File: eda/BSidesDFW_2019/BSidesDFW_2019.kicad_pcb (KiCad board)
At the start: 2 copper layers, 33 x 43.5 mm, 28 parts, among them IC1 CH552G, J1 USB_B_Micro, J2 Test 1-8, J3 Test 9-16, J4 Battery, SW1 TS2306A, SW11 TS2306A, SW34 TS2306A

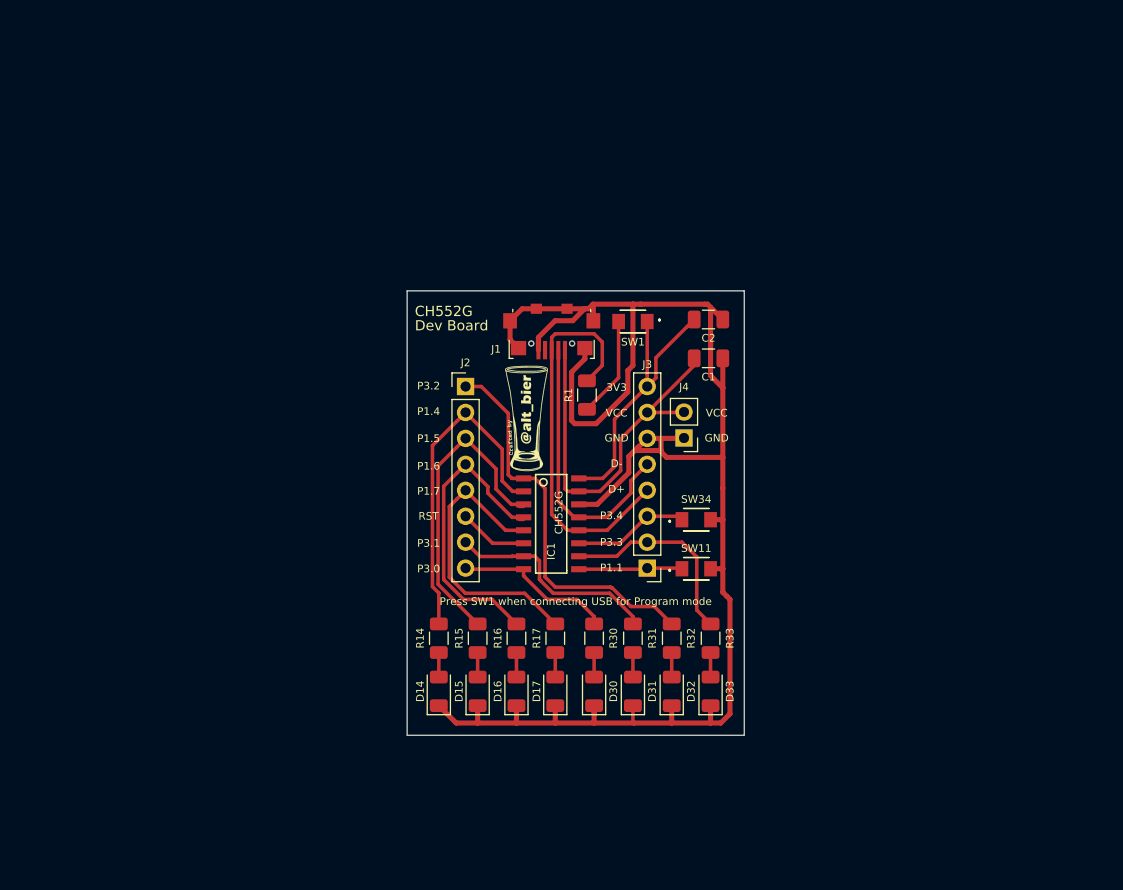
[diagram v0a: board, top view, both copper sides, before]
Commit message: Completed edge cuts for badge PCB
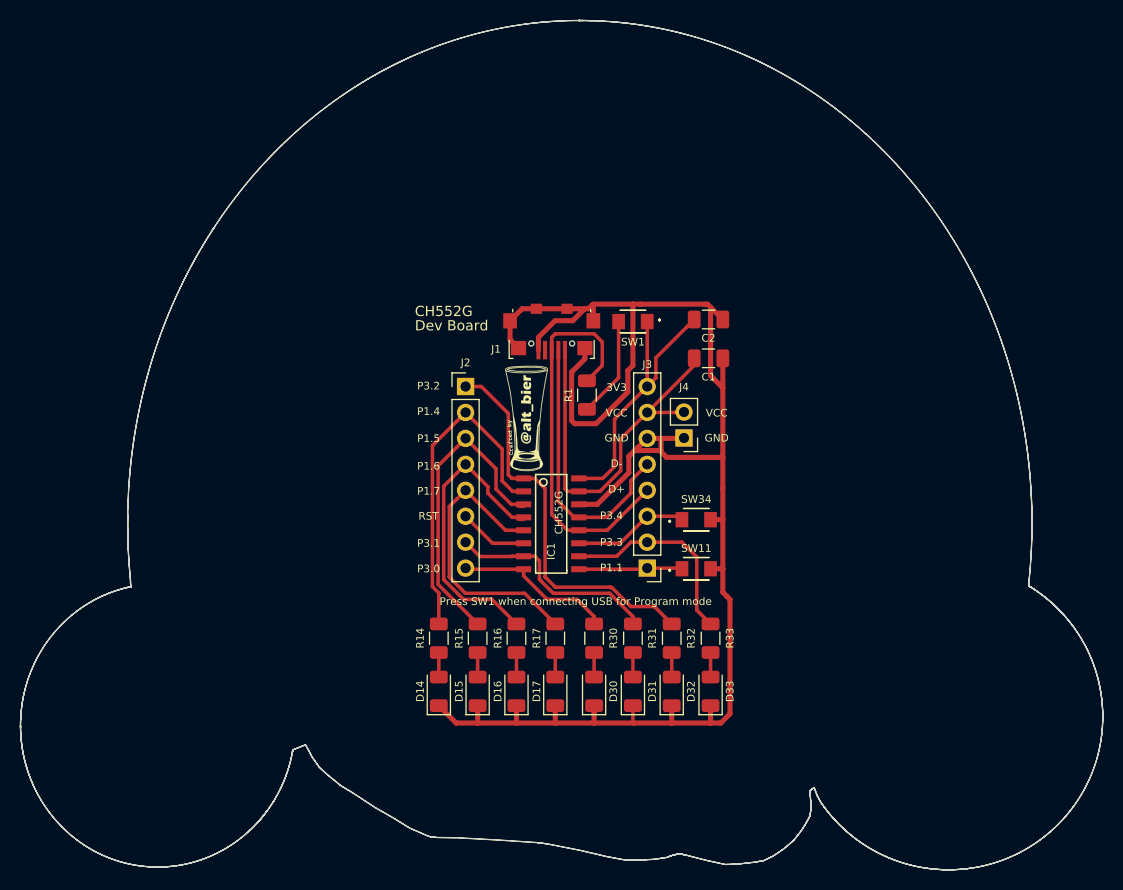
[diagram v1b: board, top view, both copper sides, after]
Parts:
- added G***: LOGO, BSidesDFW_2019:Edge_Cuts_150ppi_to_700dpi, F.Cu at (111.2, 89.6)
- C1, C2: footprint BSidesDFW_2019::C_1206_3216Metric -> BSidesDFW_2019:_C_1206_3216Metric
- D14, D15, D16, D17, D30, D31, D32, D33: footprint BSidesDFW_2019::LED_1206_3216Metric -> BSidesDFW_2019:_LED_1206_3216Metric
- IC1: footprint BSidesDFW_2019::SOIC-16_3.9x9.9mm_Pitch1.27mm -> BSidesDFW_2019:_SOIC-16_3.9x9.9mm_Pitch1.27mm
- J1: footprint BSidesDFW_2019::USB_Micro-B_Jing -> BSidesDFW_2019:_USB_Micro-B_Jing
- J2, J3: footprint BSidesDFW_2019::Pin_Header_Straight_1x08_Pitch2.54mm -> BSidesDFW_2019:_Pin_Header_Straight_1x08_Pitch2.54mm
- J4: footprint BSidesDFW_2019::Pin_Header_Straight_1x02_Pitch2.54mm -> BSidesDFW_2019:_Pin_Header_Straight_1x02_Pitch2.54mm
- R1, R14, R15, R16, R17, R30, R31, R32, R33: footprint BSidesDFW_2019::R_1206_3216Metric -> BSidesDFW_2019:_R_1206_3216Metric
- SW1, SW11, SW34: footprint BSidesDFW_2019::TS2306A240GFMSM9_C388290 -> BSidesDFW_2019:_TS2306A240GFMSM9_C388290
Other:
- board size 33 x 43.5 mm -> 105.9 x 83.1 mm

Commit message: First pass of badge pcb complete
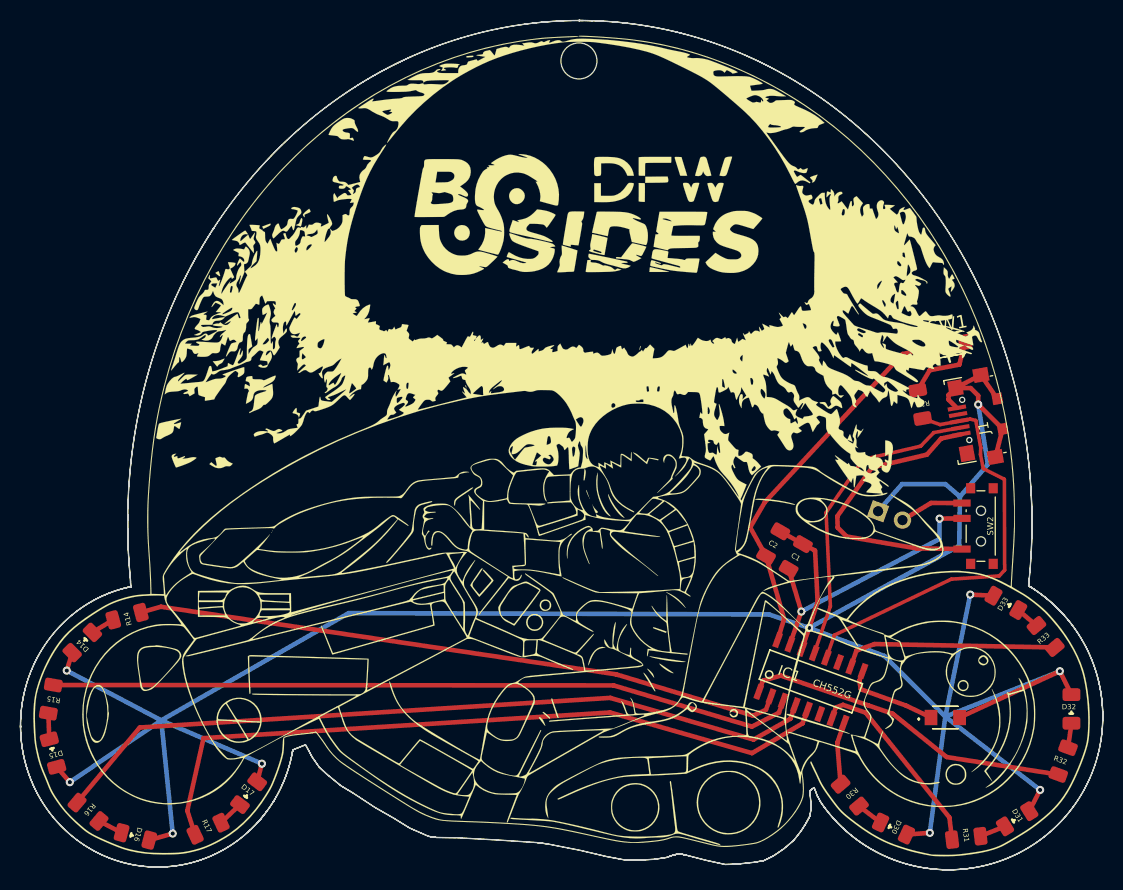
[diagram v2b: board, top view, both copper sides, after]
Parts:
- removed the G*** at (111.2, 89.6)
- removed the G*** at (106.2, 90.5)
- removed J3: Test 9-16, BSidesDFW_2019:_Pin_Header_Straight_1x08_Pitch2.54mm
- removed J4: Battery, BSidesDFW_2019:_Pin_Header_Straight_1x02_Pitch2.54mm
- removed SW34: TS2306A, BSidesDFW_2019:_TS2306A240GFMSM9_C388290
- added G***: LOGO, BSidesDFW_2019:Akira_Badge_Art_150ppi_to_700dpi, F.Cu at (109.6, 92.9)
- added G***: LOGO, BSidesDFW_2019:Outlines_150ppi_to_700dpi, F.Cu at (109.6, 93.1)
- added SW2: SW_SPDT_C136659, BSidesDFW_2019:SW_SPDT_PCM12_C136659, F.Cu at (150.6, 101.0)
- C1, C2: footprint BSidesDFW_2019:_C_1206_3216Metric -> BSidesDFW_2019:C_1206_3216Metric
- D14, D15, D16, D17, D30, D31, D32, D33: footprint BSidesDFW_2019:_LED_1206_3216Metric -> BSidesDFW_2019:LED_1206_3216Metric
- IC1: footprint BSidesDFW_2019:_SOIC-16_3.9x9.9mm_Pitch1.27mm -> BSidesDFW_2019:SOIC-16_3.9x9.9mm_Pitch1.27mm
- J1: footprint BSidesDFW_2019:_USB_Micro-B_Jing -> BSidesDFW_2019:USB_Micro-B_Jing
- J2: value Test 1-8 -> Battery; footprint BSidesDFW_2019:_Pin_Header_Straight_1x08_Pitch2.54mm -> BSidesDFW_2019:Pin_Header_Straight_1x02_Pitch2.54mm
- R1, R14, R15, R16, R17, R30, R31, R32, R33: footprint BSidesDFW_2019:_R_1206_3216Metric -> BSidesDFW_2019:R_1206_3216Metric
- SW1, SW11: footprint BSidesDFW_2019:_TS2306A240GFMSM9_C388290 -> BSidesDFW_2019:TS2306A240GFMSM9_C388290
- moved R16 45.3 mm to (63.3, 129.0), turned to 140 degrees
- moved J1 42.8 mm to (150.6, 90.4), turned to 100 degrees
- moved R15 42.2 mm to (59.6, 118.0), turned to 80 degrees
- moved J2 42.2 mm to (140.6, 99.6), turned to 70 degrees
- moved D15 42.0 mm to (59.8, 123.2), turned to 105 degrees
- moved R32 40.2 mm to (158.7, 124.0), turned to 250 degrees
- moved D16 39.9 mm to (67.9, 131.4), turned to 165 degrees
- moved D31 39.6 mm to (154.2, 129.7), turned to 212 degrees
- moved D32 39.2 mm to (159.5, 118.9), turned to 270 degrees
- moved R17 38.8 mm to (75.0, 130.7), turned to 205 degrees
- moved R31 38.0 mm to (149.2, 131.6), turned to 187 degrees
- moved D14 35.2 mm to (62.7, 112.4), turned to 45 degrees
- moved R33 32.8 mm to (157.0, 111.8), turned to 310 degrees
- moved R1 32.6 mm to (144.7, 89.1), turned to 100 degrees
- moved D30 32.2 mm to (142.1, 130.6), turned to 155 degrees
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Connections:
- J1 pad 1: VCC -> USB-PWR
- J2 pad 1: P3.2 -> GND
- J2 pad 2: P1.4 -> BAT-PWR
- R33 pad 1: P3.3 -> Net-(D33-Pad2)
- R33 pad 2: Net-(D33-Pad2) -> P3.3
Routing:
- net GND: track 168.9 -> 274.5 mm, vias 0 -> 10
- net P1.6: track 29.7 -> 75.9 mm
- net P1.7: track 28.7 -> 71.3 mm
- net P1.5: track 30.8 -> 73.2 mm
- net P1.4: track 33.0 -> 63.9 mm
- net USB-PWR: track 0.00 -> 29.3 mm
- net P3.4: track 11.3 -> 0.00 mm
- net VCC: track 37.6 -> 27.2 mm, vias 0 -> 2
- net 3V3: track 28.0 -> 37.8 mm
- net P3.0: track 15.7 -> 6.13 mm
- net RST: track 6.78 -> 0.00 mm
- net BAT-PWR: track 0.00 -> 6.29 mm
- net P3.2: track 38.4 -> 32.4 mm
- net D-: track 27.0 -> 30.7 mm
- net D+: track 38.8 -> 41.9 mm
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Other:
- outline, holes or cut-outs redrawn
- board text removed: "3V3"
- board text removed: "CH552G"
- board text removed: "D+"
- board text removed: "D-"
- board text removed: "Dev Board"
- board text removed: "GND"
- board text removed: "P1.1"
- board text removed: "P1.4"
- board text removed: "P1.5"
- board text removed: "P1.6"
- board text removed: "P1.7"
- board text removed: "P3.0"
- board text removed: "P3.1"
- board text removed: "P3.2"
- board text removed: "P3.3"
- board text removed: "P3.4"
- board text removed: "Press SW1 when connecting USB for Program mode"
- board text removed: "RST"
- board text removed: "VCC"

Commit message: Final design pass of badge PCB
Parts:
- removed the G*** at (109.6, 93.1)
- added G***: LOGO, BSidesDFW_2019:MadHat_Logo_150ppi_to_2600dpi, F.Cu at (150.0, 118.6)
- added G***: LOGO, BSidesDFW_2019:DDI_Logo_700dpi_Back, F.Cu at (109.1, 70.1)
- added G***: LOGO, alt_bier:logo-alt_bier-800dpi-12x28mm-back, F.Cu at (74.8, 113.4)
- added REF**: BatteryHolder_3xAAA, BSidesDFW_2019:BatteryHolder_3xAAA, F.Cu at (86.8, 87.9)
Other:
- outline, holes or cut-outs redrawn
- board text added: "Hold SW1 while connecting to USB for IC Program Mode Toggle SW2 for Battery or USB Power Source Press SW11 to change Program Modes"
